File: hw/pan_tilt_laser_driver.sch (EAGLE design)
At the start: 43 parts, among them IC1 93C46, J1 POWER_JACKPTH, U1 CAT6219-330TDGT3, U2 LD3985M30R, X1 538-47346-0001, Y1 405I35D12M00000

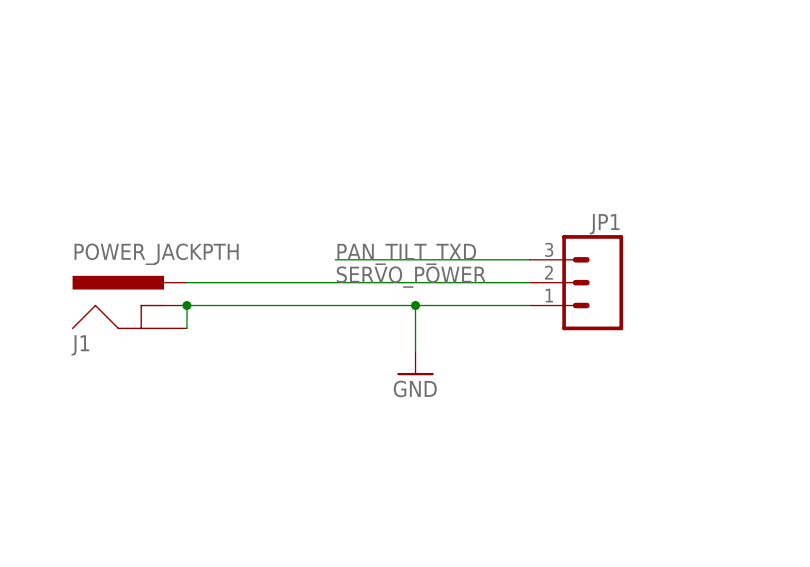
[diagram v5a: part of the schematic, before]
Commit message: Servo connector was backwards. Fixed in schematic and layout.
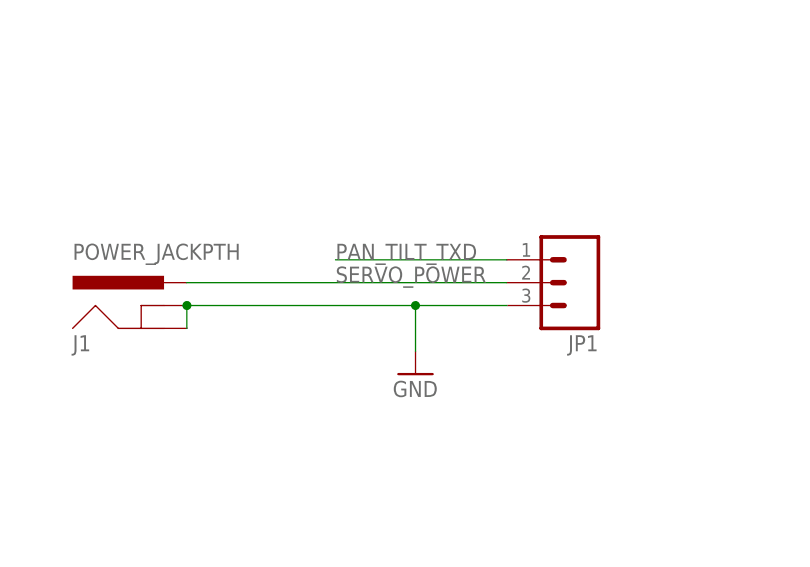
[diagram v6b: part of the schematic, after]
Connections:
- net GND: now also JP1.3; no longer JP1.1
- net PAN_TILT_TXD: now also JP1.1; no longer JP1.3
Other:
- moved on the sheet: JP1
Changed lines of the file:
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@@
 <instance part="C16" gate="G$1" x="109.22" y="96.52" rot="R90"/>
 <instance part="J1" gate="G$1" x="-73.66" y="157.48"/>
-<instance part="JP1" gate="G$1" x="-25.4" y="165.1" rot="MR0"/>
+<instance part="JP1" gate="G$1" x="-27.94" y="165.1" rot="R180"/>
 <instance part="Y1" gate="G$1" x="119.38" y="101.6" rot="R90"/>
 <instance part="U1" gate="G$1" x="66.04" y="38.1"/>
@@
 </segment>
 <segment>
-<wire x1="-33.02" y1="162.56" x2="-45.72" y2="162.56" width="0.1524" layer="91"/>
 <pinref part="GND1" gate="1" pin="GND"/>
+<wire x1="-35.56" y1="162.56" x2="-45.72" y2="162.56" width="0.1524" layer="91"/>
 <wire x1="-45.72" y1="157.48" x2="-45.72" y2="162.56" width="0.1524" layer="91"/>
 <pinref part="J1" gate="G$1" pin="GND"/>
@@
 <junction x="-71.12" y="162.56"/>
 <junction x="-45.72" y="162.56"/>
-<pinref part="JP1" gate="G$1" pin="1"/>
+<pinref part="JP1" gate="G$1" pin="3"/>
 </segment>
 <segment>
@@
 </segment>
 <segment>
-<wire x1="-33.02" y1="167.64" x2="-54.61" y2="167.64" width="0.1524" layer="91"/>
 <label x="-54.61" y="167.64" size="1.778" layer="95"/>
-<pinref part="JP1" gate="G$1" pin="3"/>
+<wire x1="-35.56" y1="167.64" x2="-54.61" y2="167.64" width="0.1524" layer="91"/>
+<pinref part="JP1" gate="G$1" pin="1"/>
 </segment>
 </net>
@@
 <label x="-54.61" y="165.1" size="1.778" layer="95"/>
 <pinref part="J1" gate="G$1" pin="PWR"/>
-<wire x1="-71.12" y1="165.1" x2="-33.02" y2="165.1" width="0.1524" layer="91"/>
+<wire x1="-71.12" y1="165.1" x2="-35.56" y2="165.1" width="0.1524" layer="91"/>
 <pinref part="JP1" gate="G$1" pin="2"/>
 </segment>
